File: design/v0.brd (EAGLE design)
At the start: 100 x 62 mm, 30 parts, among them U1 CHERRY-MX, U2 CHERRY-MX, U3 CHERRY-MX, U4 CHERRY-MX, U5 CHERRY-MX, U6 CHERRY-MX, U7 CHERRY-MX, U8 CHERRY-MX, U9 CHERRY-MX

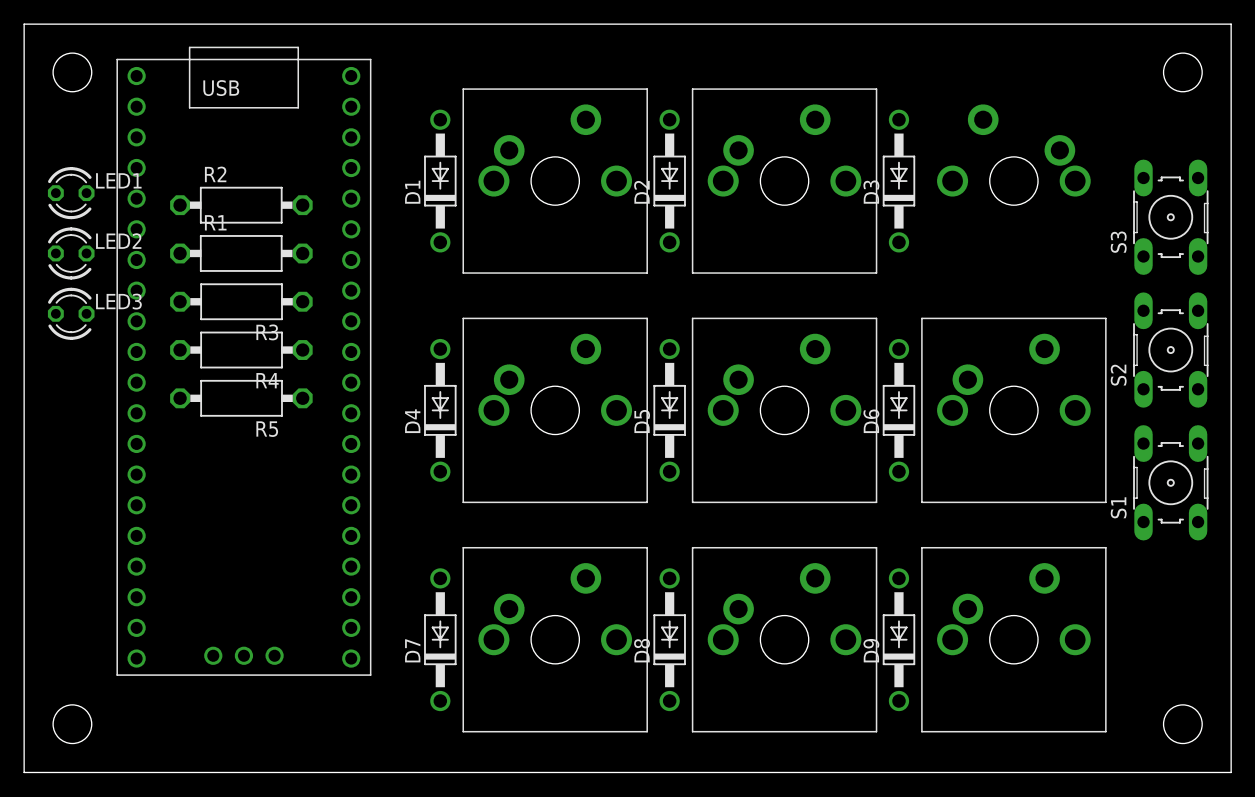
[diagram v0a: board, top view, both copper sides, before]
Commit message: Add silkscreen text, move labels, perform routing
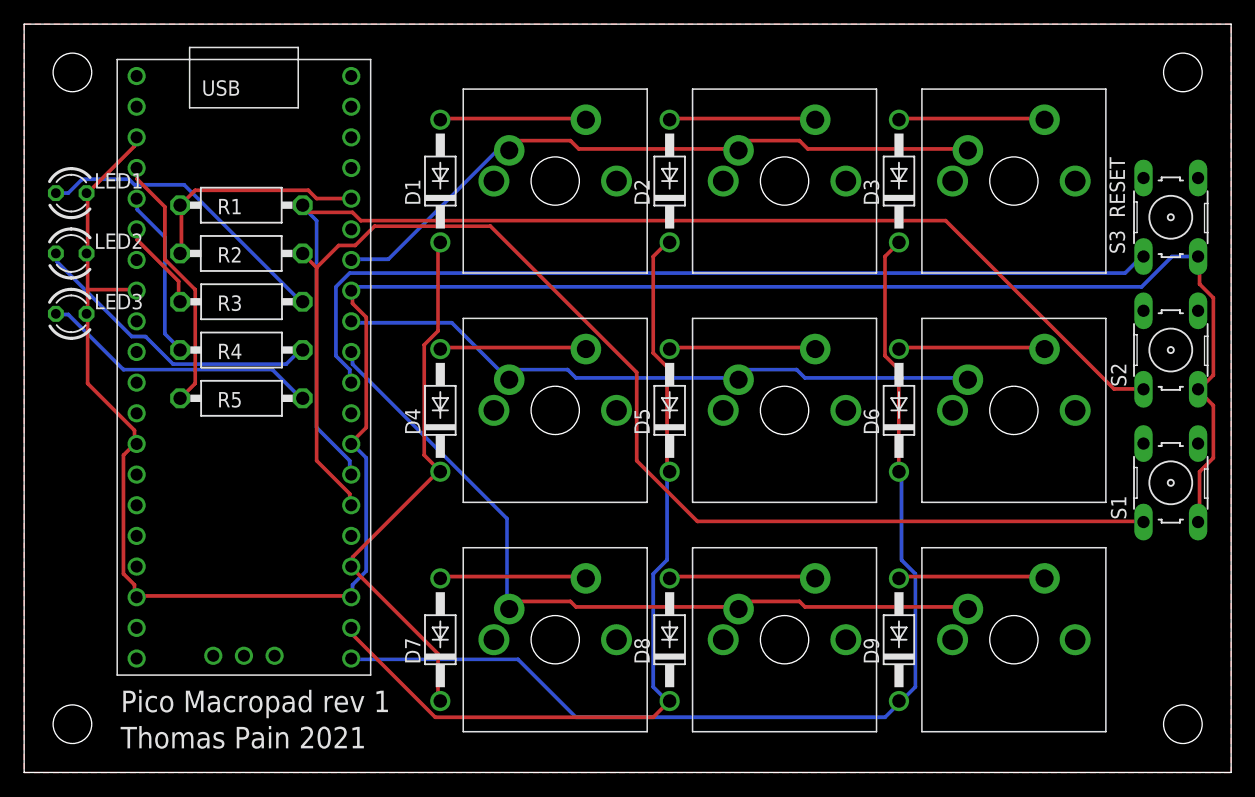
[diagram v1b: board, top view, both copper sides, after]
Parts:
- moved R1 4.00 mm to (18.0, 47.0)
- moved R2 4.00 mm to (18.0, 43.0)
- flipped U3 to the top
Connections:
- net N$4: now also R1.2; no longer R2.2
- net N$9: now also R2.2; no longer R1.2
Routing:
- net GND: track 0.00 -> 187.8 mm
- net N$9: track 0.00 -> 106.9 mm
- net N$4: track 0.00 -> 100.1 mm
- net N$17: track 0.00 -> 88.4 mm
- net N$13: track 0.00 -> 76.4 mm
- net N$16: track 0.00 -> 70.8 mm
- net N$29: track 0.00 -> 66.0 mm
- net N$27: track 0.00 -> 56.3 mm
- net N$28: track 0.00 -> 54.7 mm
- net N$15: track 0.00 -> 45.5 mm
- net N$1: track 0.00 -> 25.1 mm
- net N$2: track 0.00 -> 25.1 mm
- net N$3: track 0.00 -> 23.3 mm
- net N$5: track 0.00 -> 21.6 mm
- net N$12: track 0.00 -> 19.0 mm
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- added copper zone on layer 1, net GND
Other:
- board text added: "JLCJLCJLCJLC"
- board text added: "Pico Macropad rev 1"
- board text added: "Thomas Pain 2021"

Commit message: Silkscreen tweaks
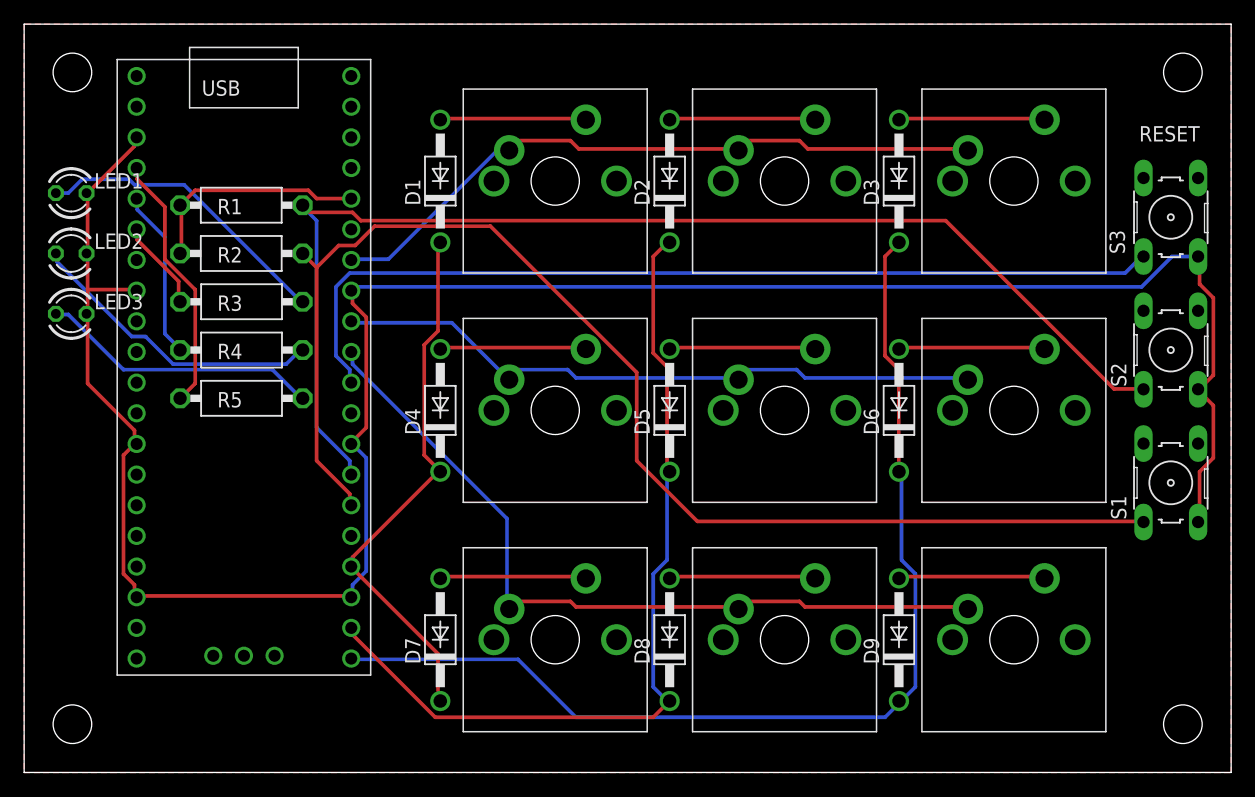
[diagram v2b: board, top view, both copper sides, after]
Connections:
- net GND: now also U$1.38
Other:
- board text added: "001"
- board text added: "Macropad rev 0 Jan 2021"
- board text removed: "Pico Macropad rev 1"
- board text removed: "Thomas Pain 2021"
